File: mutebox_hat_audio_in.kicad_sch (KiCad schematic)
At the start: 23 parts, among them J1 GPIO, U1 CAT24C256, U2 74LVC157, U3 PCM1862DBT

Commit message: Started on PCB
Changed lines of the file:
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@@
 	(wire
 		(pts
-			(xy 134.62 41.91) (xy 137.16 41.91)
+			(xy 135.89 41.91) (xy 137.16 41.91)
 		)
 		(stroke
@@
 	(wire
 		(pts
-			(xy 134.62 44.45) (xy 137.16 44.45)
+			(xy 135.89 44.45) (xy 137.16 44.45)
 		)
 		(stroke
@@
 	(wire
 		(pts
-			(xy 134.62 36.83) (xy 137.16 36.83)
+			(xy 135.89 36.83) (xy 137.16 36.83)
 		)
 		(stroke
@@
 	(wire
 		(pts
-			(xy 134.62 34.29) (xy 137.16 34.29)
+			(xy 135.89 34.29) (xy 137.16 34.29)
 		)
 		(stroke
@@
 	(global_label "ADC_LRCLK"
 		(shape input)
-		(at 134.62 44.45 180)
+		(at 135.89 44.45 180)
 		(fields_autoplaced yes)
 		(effects
@@
 		)
 		(property "Intersheetrefs" "${INTERSHEET_REFS}"
-			(at 148.1627 44.45 0)
+			(at 149.4327 44.45 0)
 			(effects
 				(font
@@
 	(global_label "ADC_BCLK"
 		(shape input)
-		(at 134.62 36.83 180)
+		(at 135.89 36.83 180)
 		(fields_autoplaced yes)
 		(effects
@@
 		)
 		(property "Intersheetrefs" "${INTERSHEET_REFS}"
-			(at 122.1054 36.83 0)
+			(at 123.3754 36.83 0)
 			(effects
 				(font
@@
 	(global_label "TOSLINK_BCLK"
 		(shape input)
-		(at 134.62 34.29 180)
+		(at 135.89 34.29 180)
 		(fields_autoplaced yes)
 		(effects
@@
 		)
 		(property "Intersheetrefs" "${INTERSHEET_REFS}"
-			(at 117.993 34.29 0)
+			(at 119.263 34.29 0)
 			(effects
 				(font
@@
 	(global_label "TOSLINK_LRCLK"
 		(shape input)
-		(at 134.62 41.91 180)
+		(at 135.89 41.91 180)
 		(fields_autoplaced yes)
 		(effects
@@
 		)
 		(property "Intersheetrefs" "${INTERSHEET_REFS}"
-			(at 116.9649 41.91 0)
+			(at 118.2349 41.91 0)
 			(effects
 				(font
@@
 		(dnp no)
 		(property "Reference" "U2"
-			(at 152.0033 26.67 0)
+			(at 151.765 27.94 0)
 			(effects
 				(font
@@
 		)
 		(property "Value" "74LVC157"
-			(at 152.0033 29.21 0)
+			(at 151.765 30.48 0)
 			(effects
 				(font

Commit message: Added routes for crystal and part of toslink
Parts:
- J_L_IN1, J_R_IN1: footprint Connector_Coaxial:SMA_Amphenol_901-143_Horizontal -> Connector_Audio:RCJ-043
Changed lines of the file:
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@@
 			)
 		)
-		(property "Footprint" "Connector_Coaxial:SMA_Amphenol_901-143_Horizontal"
+		(property "Footprint" "Connector_Audio:RCJ-043"
 			(at 100.965 102.87 0)
 			(effects
@@
 			)
 		)
-		(property "Footprint" "Connector_Coaxial:SMA_Amphenol_901-143_Horizontal"
+		(property "Footprint" "Connector_Audio:RCJ-043"
 			(at 100.965 121.92 0)
 			(effects

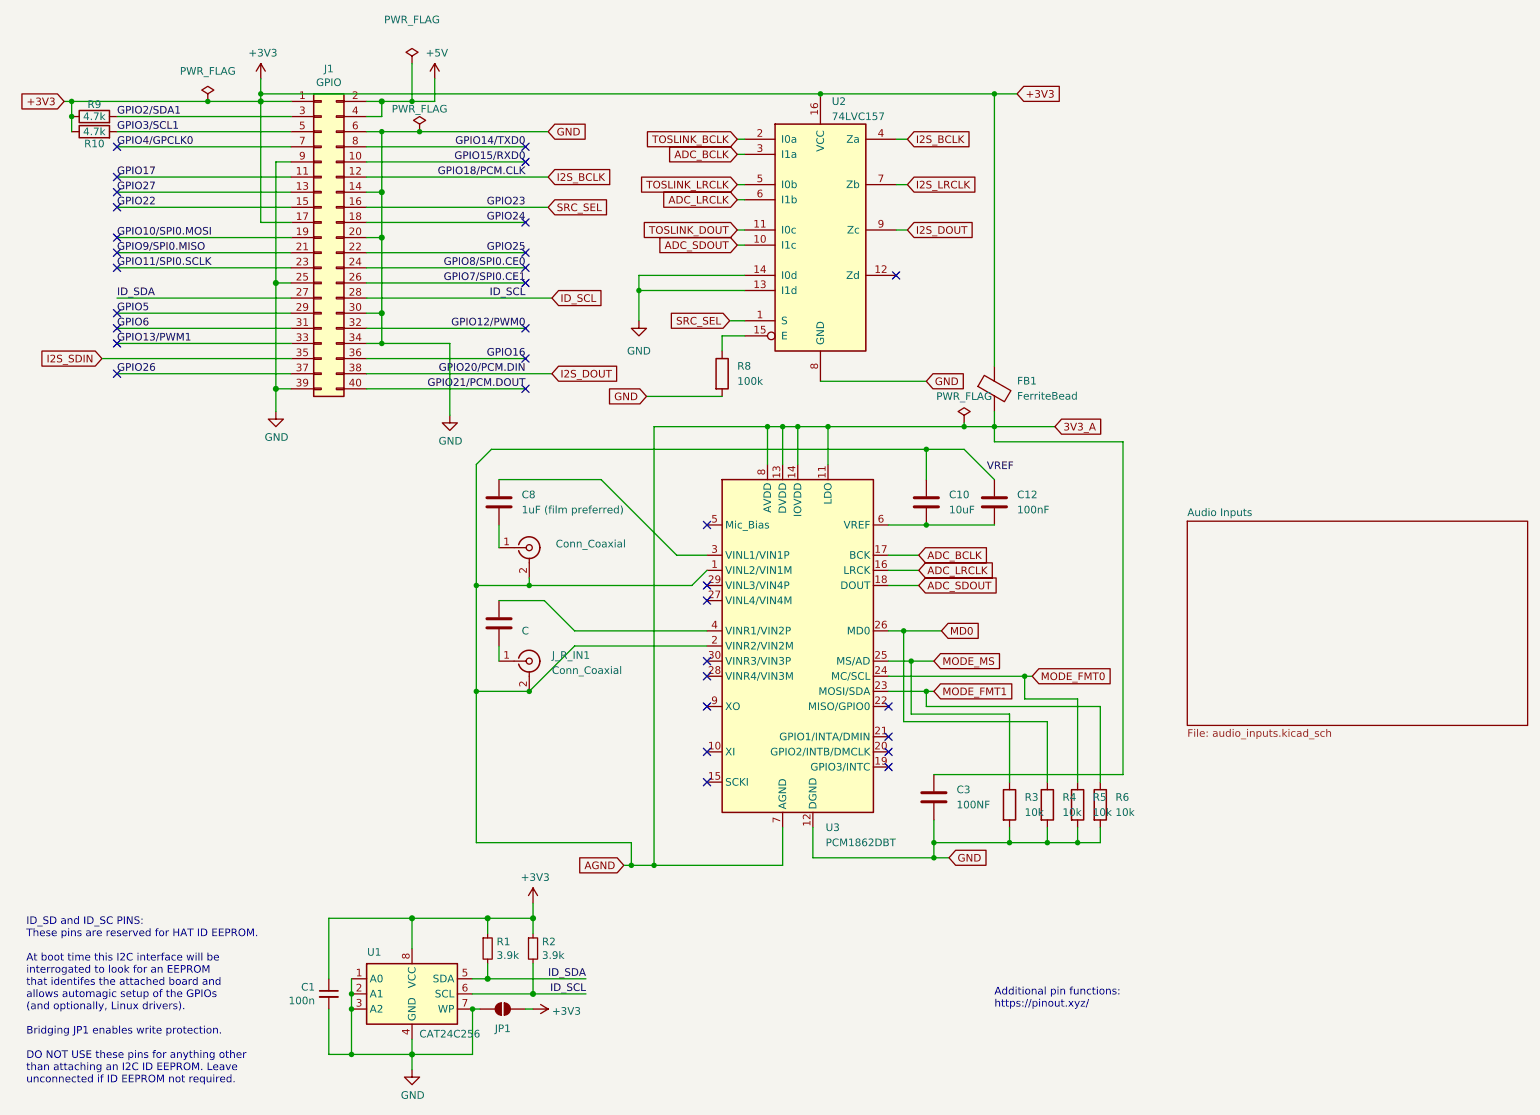
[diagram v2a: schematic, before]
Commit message: Added better multiplexer setup
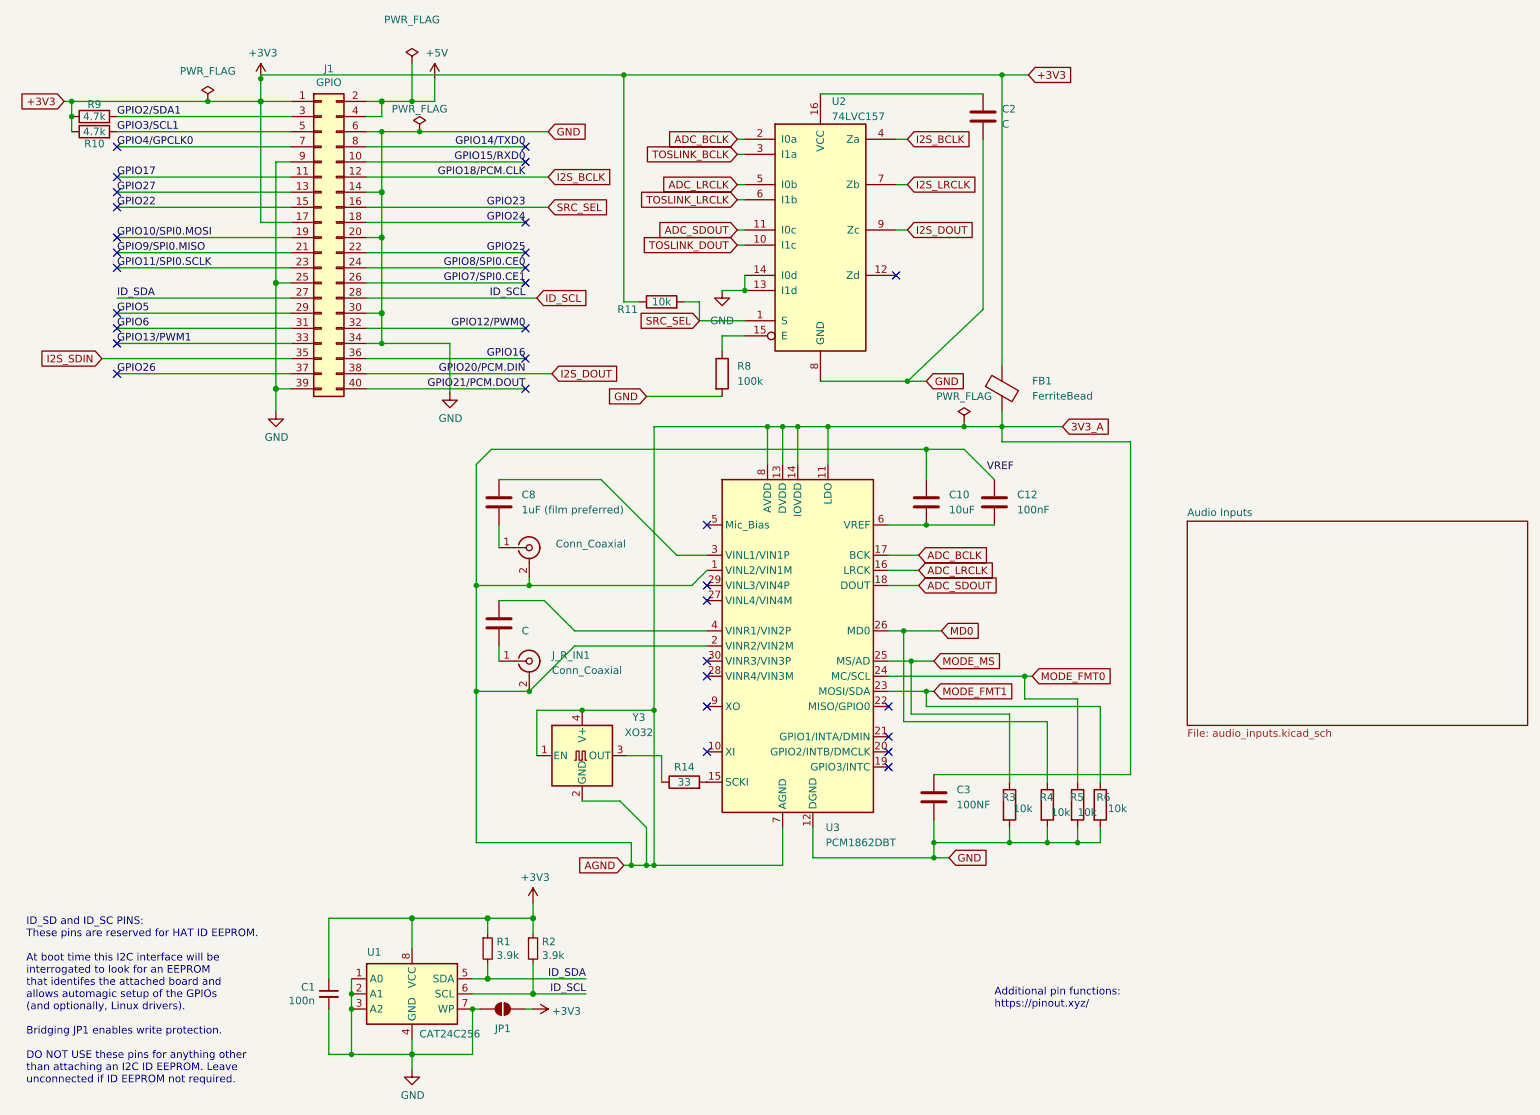
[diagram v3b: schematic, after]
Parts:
- added C2: C, symbol Device:C
- added R11: 10k, symbol Device:R
- added R14: 33, symbol Device:R
- added Y3: XO32, Oscillator:Oscillator_SMD_EuroQuartz_XO32-4Pin_3.2x2.5mm, symbol Oscillator:XO32
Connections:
- net +3V3: now also R11.1; no longer U2.16 (VCC)
- net 3V3_A: now also Y3.1 (EN), Y3.2 (GND), Y3.4 (V+)
- net ADC_BCLK: now also U2.2 (I0a); no longer U2.3 (I1a)
- net ADC_LRCLK: now also U2.5 (I0b); no longer U2.6 (I1b)
- net ADC_SDOUT: now also U2.11 (I0c); no longer U2.10 (I1c)
- net GND: now also C2.2
- net SRC_SEL: now also R11.2
- net TOSLINK_BCLK: now also U2.3 (I1a); no longer U2.2 (I0a)
- net TOSLINK_DOUT: now also U2.10 (I1c); no longer U2.11 (I0c)
- net TOSLINK_LRCLK: now also U2.6 (I1b); no longer U2.5 (I0b)
- net at U3.15 (SCKI): now also R14.2
- new net: C2.1, U2.16 (VCC)
- new net: R14.1, Y3.3 (OUT)
- no-connect marks 33 -> 32
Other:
- moved on the sheet: FB1

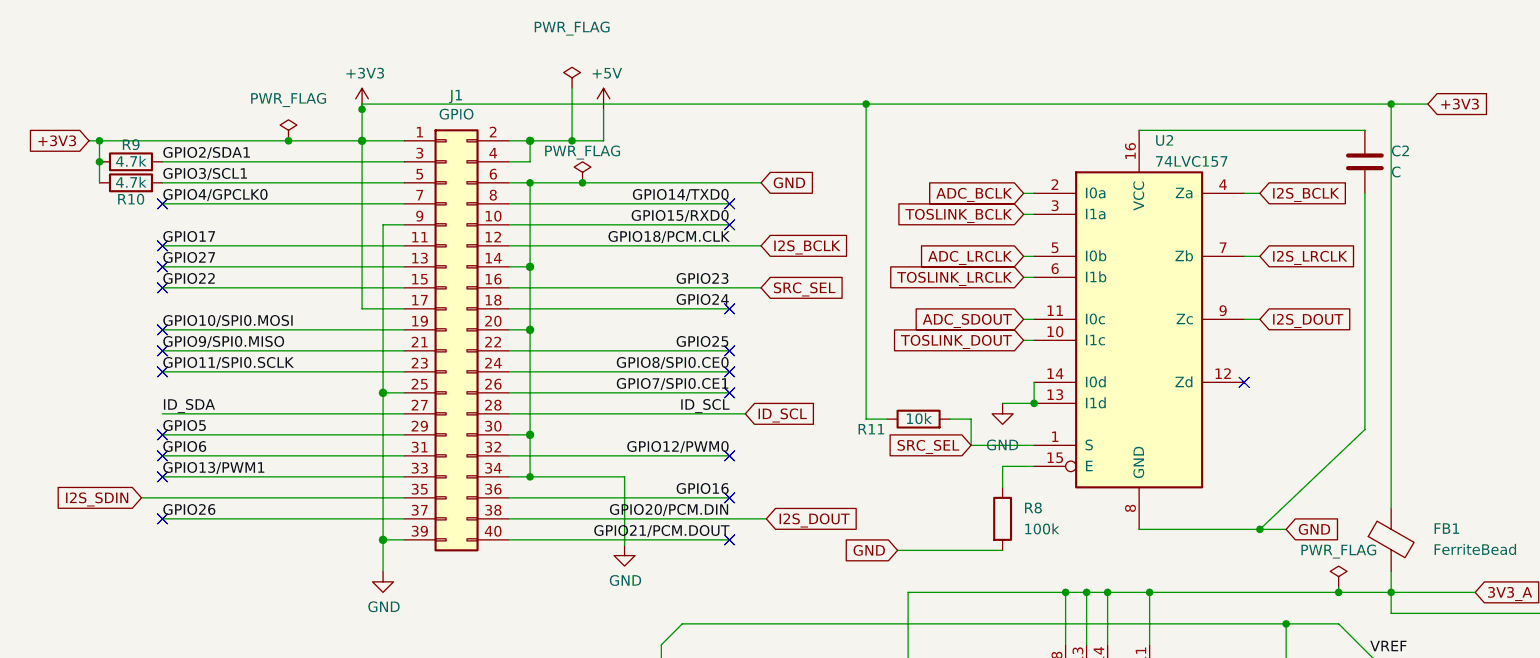
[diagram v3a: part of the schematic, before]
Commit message: Changed DIN connections
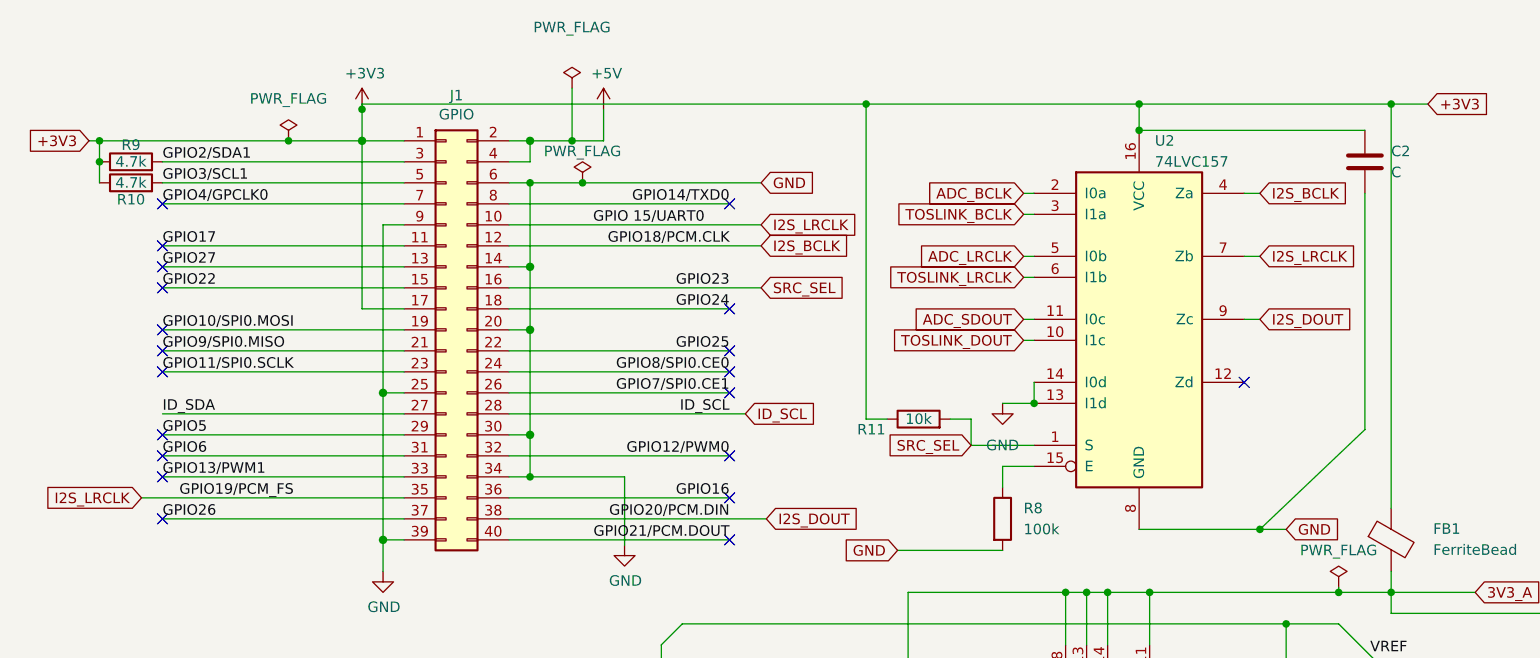
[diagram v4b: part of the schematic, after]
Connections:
- net GPIO15/RXD0 is gone; now on net I2S_LRCLK: J1.10 (Pin_10)
- net I2S_SDIN is gone; now on net I2S_LRCLK: J1.35 (Pin_35)
- net +3V3: now also C2.1, U2.16 (VCC)
- no-connect marks 32 -> 31
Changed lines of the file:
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@@
+	)
+	(junction
+		(at 149.86 23.495)
+		(diameter 0)
+		(color 0 0 0 0)
 	)
 	(junction
@@
 	)
 	(junction
+		(at 149.86 26.67)
+		(diameter 0)
+		(color 0 0 0 0)
+	)
+	(junction
 		(at 173.99 82.55)
 		(diameter 0)
@@
 	)
 	(no_connect
-		(at 100.33 38.1)
-	)
-	(no_connect
 		(at 31.75 35.56)
 	)
@@
 	(wire
 		(pts
-			(xy 73.66 38.1) (xy 100.33 38.1)
+			(xy 73.66 38.1) (xy 104.14 38.1)
 		)
 		(stroke
@@
 	(wire
 		(pts
+			(xy 149.86 23.495) (xy 149.86 26.67)
+		)
+		(stroke
+			(width 0)
+			(type default)
+		)
+	)
+	(wire
+		(pts
 			(xy 137.16 57.15) (xy 137.16 59.69)
 		)
@@
 	(wire
 		(pts
+			(xy 149.86 23.495) (xy 180.34 23.495)
+		)
+		(stroke
+			(width 0)
+			(type default)
+		)
+	)
+	(wire
+		(pts
 			(xy 149.86 74.93) (xy 164.465 74.93)
 		)
@@
 	(wire
 		(pts
-			(xy 116.84 23.495) (xy 180.34 23.495)
+			(xy 116.84 23.495) (xy 149.86 23.495)
 		)
 		(stroke
@@
 		)
 	)
+	(label "GPIO19{slash}PCM_FS"
+		(at 47.625 71.12 180)
+		(effects
+			(font
+				(size 1.27 1.27)
+			)
+			(justify right bottom)
+		)
+	)
 	(label "GPIO4{slash}GPCLK0"
 		(at 31.75 35.56 0)
@@
 		)
 	)
-	(label "GPIO15{slash}RXD0"
-		(at 100.33 38.1 180)
-		(effects
-			(font
-				(size 1.27 1.27)
-			)
-			(justify right bottom)
-		)
-	)
 	(label "GPIO16"
 		(at 100.33 71.12 180)
@@
 			)
 			(justify right bottom)
+		)
+	)
+	(label "GPIO 15{slash}UART0"
+		(at 83.82 38.1 0)
+		(effects
+			(font
+				(size 1.27 1.27)
+			)
+			(justify left bottom)
 		)
 	)
@@
 		)
 	)
+	(global_label "I2S_LRCLK"
+		(shape input)
+		(at 104.14 38.1 0)
+		(fields_autoplaced yes)
+		(effects
+			(font
+				(size 1.27 1.27)
+			)
+			(justify left)
+		)
+		(property "Intersheetrefs" "${INTERSHEET_REFS}"
+			(at 117.0779 38.1 0)
+			(effects
+				(font
+					(size 1.27 1.27)
+				)
+				(justify left)
+				(hide yes)
+			)
+		)
+	)
 	(global_label "ADC_BCLK"
 		(shape input)
@@
 		)
 	)
-	(global_label "I2S_SDIN"
+	(global_label "I2S_LRCLK"
 		(shape input)
 		(at 29.21 71.12 180)
@@
 		)
 		(property "Intersheetrefs" "${INTERSHEET_REFS}"
-			(at 40.6965 71.12 0)
+			(at 16.2721 71.12 0)
 			(effects
 				(font
 					(size 1.27 1.27)
 				)
-				(justify left)
+				(justify right)
 				(hide yes)
 			)

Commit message: Fixed a bunch of schematic issues
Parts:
- removed R11: 10k, symbol Device:R
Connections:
- net 3V3_A: no longer C10.1, C12.1, J_L_IN1.2 (Ext), J_R_IN1.2 (Ext), U3.1 (VINL2/VIN1M), U3.2 (VINR2/VIN2M), U3.7 (AGND), Y3.1 (EN), Y3.2 (GND), Y3.4 (V+)
- net GND: now also C10.2, C12.2
- net I2S_LRCLK: no longer J1.10 (Pin_10)
- net SRC_SEL renamed GPIO23_OPT_LOCK
- new net AGND: U3.7 (AGND), Y3.1 (EN), Y3.2 (GND), Y3.4 (V+)
- new net VREF: C10.1, C12.1, J_L_IN1.2 (Ext), J_R_IN1.2 (Ext), U3.1 (VINL2/VIN1M), U3.2 (VINR2/VIN2M), U3.6 (VREF)
- no-connect marks 31 -> 32

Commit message: More routing on PCB
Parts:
- C2: footprint (none) -> Capacitor_SMD:C_0805_2012Metric_Pad1.18x1.45mm_HandSolder
- R14: footprint (none) -> Resistor_SMD:R_0805_2012Metric_Pad1.20x1.40mm_HandSolder
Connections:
- net AGND is gone; now on net GND: U3.7 (AGND), Y3.1 (EN), Y3.2 (GND), Y3.4 (V+)
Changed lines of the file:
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@@
 	)
 	(junction
-		(at 120.65 156.21)
-		(diameter 0)
-		(color 0 0 0 0)
-	)
-	(junction
 		(at 76.2 63.5)
 		(diameter 1.016)
@@
 	)
 	(junction
+		(at 143.51 156.21)
+		(diameter 0)
+		(color 0 0 0 0)
+	)
+	(junction
 		(at 91.44 180.34)
 		(diameter 0)
@@
 	(wire
 		(pts
-			(xy 116.84 156.21) (xy 120.65 156.21)
-		)
-		(stroke
-			(width 0)
-			(type default)
-		)
-	)
-	(wire
-		(pts
 			(xy 161.29 86.36) (xy 167.64 86.36)
 		)
@@
 		)
 	)
-	(global_label "AGND"
-		(shape input)
-		(at 116.84 156.21 180)
-		(fields_autoplaced yes)
-		(effects
-			(font
-				(size 1.27 1.27)
-			)
-			(justify right)
-		)
-		(property "Intersheetrefs" "${INTERSHEET_REFS}"
-			(at 124.8794 156.21 0)
-			(effects
-				(font
-					(size 1.27 1.27)
-				)
-				(justify left)
-				(hide yes)
-			)
-		)
-	)
 	(global_label "ADC_LRCLK"
 		(shape input)
@@
 	)
 	(symbol
+		(lib_id "power:GND")
+		(at 143.51 156.21 0)
+		(unit 1)
+		(exclude_from_sim no)
+		(in_bom yes)
+		(on_board yes)
+		(dnp no)
+		(fields_autoplaced yes)
+		(property "Reference" "#PWR09"
+			(at 143.51 162.56 0)
+			(effects
+				(font
+					(size 1.27 1.27)
+				)
+				(hide yes)
+			)
+		)
+		(property "Value" "GND"
+			(at 143.51 161.29 0)
+			(effects
+				(font
+					(size 1.27 1.27)
+				)
+			)
+		)
+		(property "Footprint" ""
+			(at 143.51 156.21 0)
+			(effects
+				(font
+					(size 1.27 1.27)
+				)
+				(hide yes)
+			)
+		)
+		(property "Datasheet" ""
+			(at 143.51 156.21 0)
+			(effects
+				(font
+					(size 1.27 1.27)
+				)
+				(hide yes)
+			)
+		)
+		(property "Description" "Power symbol creates a global label with name \"GND\" , ground"
+			(at 143.51 156.21 0)
+			(effects
+				(font
+					(size 1.27 1.27)
+				)
+				(hide yes)
+			)
+		)
+		(pin "1"
+		)
+		(instances
+			(project ""
+				(path "/e63e39d7-6ac0-4ffd-8aa3-1841a4541b55"
+					(reference "#PWR09")
+					(unit 1)
+				)
+			)
+		)
+	)
+	(symbol
 		(lib_id "power:PWR_FLAG")
 		(at 173.99 81.915 0)
@@
 			)
 		)
-		(property "Footprint" ""
+		(property "Footprint" "Capacitor_SMD:C_0805_2012Metric_Pad1.18x1.45mm_HandSolder"
 			(at 178.1302 34.29 0)
 			(effects
@@
 			)
 		)
-		(property "Footprint" ""
+		(property "Footprint" "Resistor_SMD:R_0805_2012Metric_Pad1.20x1.40mm_HandSolder"
 			(at 127 144.018 90)
 			(effects
